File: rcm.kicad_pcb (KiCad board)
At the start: 2 copper layers, 140 x 70 mm, 158 parts, among them Y1 8MHz, Y2 32.768kHz

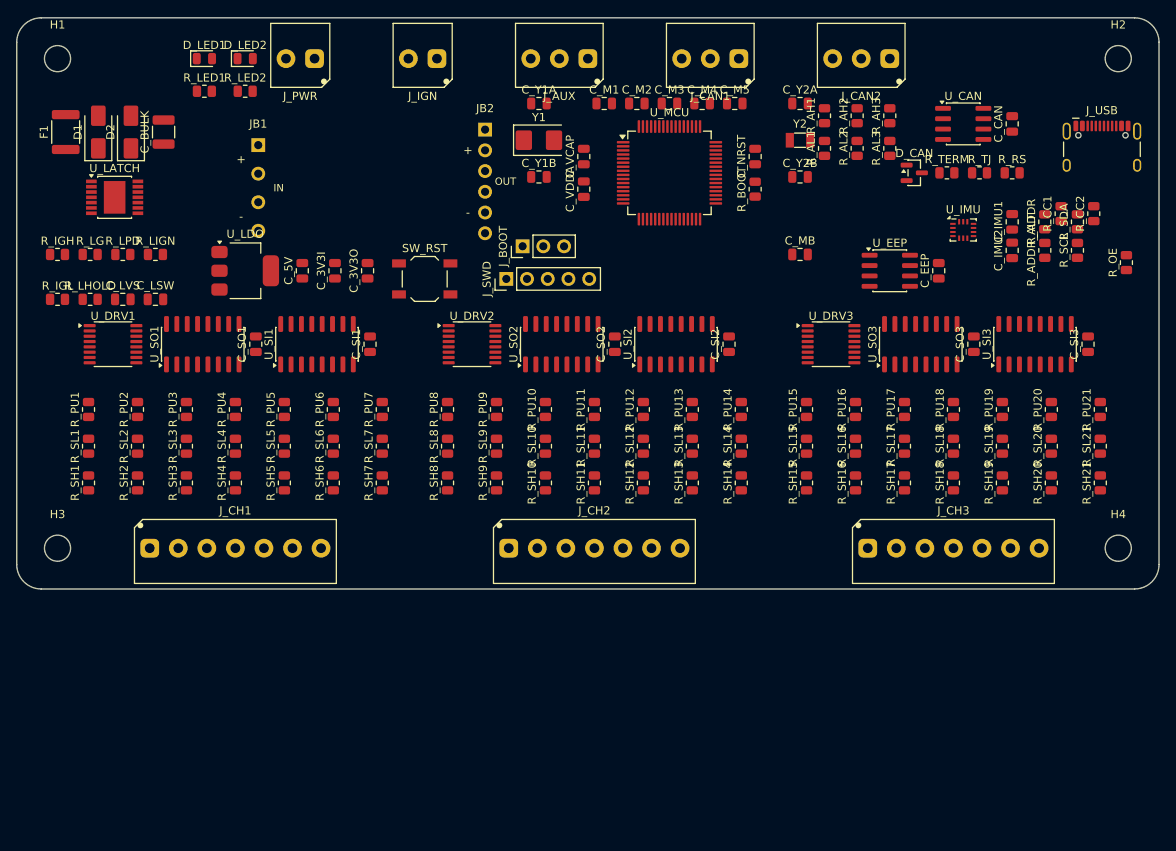
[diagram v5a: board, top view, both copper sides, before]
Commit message: rcm: board routed - 414/414 nets, 0 unconnected
Round 1 routed 413 of 414 in 63 seconds and needed NO placement changes for
congestion, which was the thing we expected to fight. The spread-out layout did
its job.

Two real issues came out of it:

- Starved thermals: a ground pad reaching the pour through one narrow neck. On
  reflow-soldered parts the relief buys nothing, so a solid connection is both
  the fix and the better design. Which pads get starved changes on every
  re-route, so fix_starved_thermals.py reads the DRC report rather than
  hard-coding them - re-run it after every route.
- USB_CC1 was unroutable: the CC pin sits in a 0.5mm-pitch pad row with no
  escape gap and I had placed its resistor on the side where the second pad row
  blocks the way. Moved to the connector's open side; round 2 then routed all
  414 nets with 0 unconnected.

Left open deliberately, per the user: rotate the USB-C 90 degrees anticlockwise
so it opens out of the east edge instead of the north. That also clears the two
remaining courtyard errors (H2 against the relocated CC resistors), so fixing
them now would be wasted work.

Co-Authored-By: Claude Opus 5 <noreply@anthropic.com>
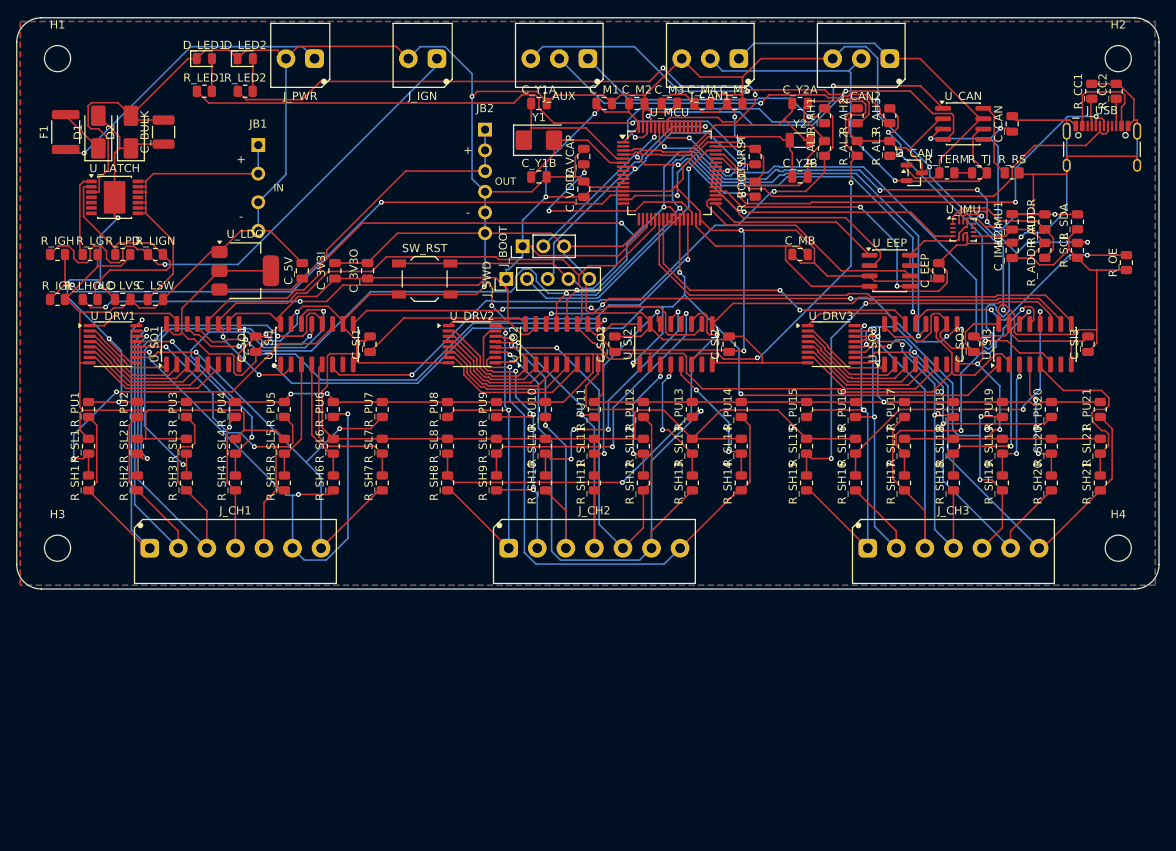
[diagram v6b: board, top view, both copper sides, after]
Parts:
- moved R_CC1 15.5 mm to (131.8, 9.00)
- moved R_CC2 15.2 mm to (134.8, 9.00)
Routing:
- net GND: track 0.00 -> 863.1 mm, vias 0 -> 10
- net +3V3: track 0.00 -> 413.6 mm, vias 0 -> 9
- net +12V_P: track 0.00 -> 214.8 mm, vias 0 -> 8
- net SR_OE_N: track 0.00 -> 159.7 mm, vias 0 -> 6
- net SR_SCK: track 0.00 -> 150.3 mm, vias 0 -> 2
- net SR_RCLK: track 0.00 -> 138.6 mm, vias 0 -> 4
- net SR_PL: track 0.00 -> 123.6 mm, vias 0 -> 4
- net IMU_SCL: track 0.00 -> 95.1 mm, vias 0 -> 3
- net LATCH_HOLD: track 0.00 -> 87.1 mm, vias 0 -> 4
- net LED2: track 0.00 -> 81.0 mm, vias 0 -> 2
- net ASNS1: track 0.00 -> 80.2 mm, vias 0 -> 2
- net IGN_SENSE: track 0.00 -> 80.1 mm, vias 0 -> 2
- net LED1: track 0.00 -> 77.0 mm, vias 0 -> 2
- net CH13: track 0.00 -> 71.3 mm, vias 0 -> 2
- net CH14: track 0.00 -> 69.0 mm, vias 0 -> 1
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- added copper zone on B.Cu, net GND
- added copper zone on F.Cu, net GND

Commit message: rcm: round 3 - USB-C rotated +90, headers and southern resistors nudged
Applies the three requested changes: J_USB rotated 0 -> +90 so it opens out of
the east edge, J_SWD and J_BOOT moved right and down to clear the buck, and all
southern resistor rows moved down 2mm to close the gap to their terminals.

Rotating the USB-C moves its CC pads, and all 16 signal pads share one local y,
so there is no asymmetry to predict orientation from. The new pad positions were
read back off the placed board rather than predicted - local pad coordinates do
not change under rotation, only the footprint angle. The CC resistors, I2C
pull-ups and CAN slope resistor all moved as a knock-on.

Routed 414/414 with 0 unconnected, 2346 segments and vias. After the usual
starved-thermal pass the board is at 0 errors.

Still unverified and worth an eyeball: which way the USB opening actually faces.
The body sits east of the pad row, which implies the cable entry is on the east
edge as intended, but that is inference not verification. If it faces inward the
fix is 270 rather than 90.

Co-Authored-By: Claude Opus 5 <noreply@anthropic.com>
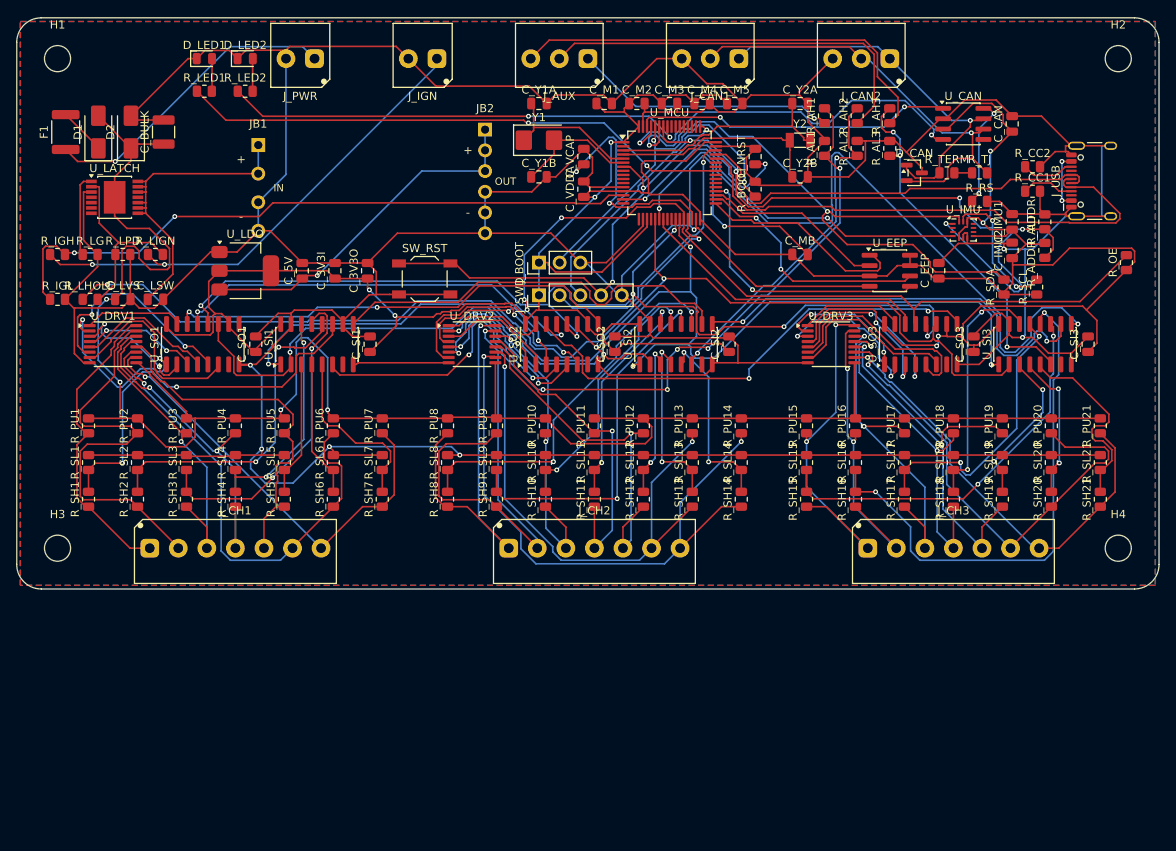
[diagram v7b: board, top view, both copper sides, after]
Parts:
- moved R_CC1 14.2 mm to (124.5, 21.2), turned to 0 degrees
- moved R_CC2 13.8 mm to (124.5, 18.2), turned to 0 degrees
- moved R_SDA 12.0 mm to (121.0, 33.0)
- moved R_SCL 6.73 mm to (125.0, 33.0)
- moved R_RS 5.32 mm to (118.0, 22.5)
- moved J_SWD 4.47 mm to (64.0, 34.0)
- moved J_USB 3.00 mm to (133.0, 20.0), turned to 90 degrees
- moved J_BOOT 2.83 mm to (64.0, 30.0)
- moved R_PU1 2.00 mm to (8.80, 50.0)
- moved R_PU10 2.00 mm to (64.8, 50.0)
- moved R_PU11 2.00 mm to (70.8, 50.0)
- moved R_PU12 2.00 mm to (76.8, 50.0)
- moved R_PU13 2.00 mm to (82.8, 50.0)
- moved R_PU14 2.00 mm to (88.8, 50.0)
- moved R_PU15 2.00 mm to (96.8, 50.0)
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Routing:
- net GND: track 863.1 -> 814.1 mm, vias 10 -> 8
- net +3V3: track 413.6 -> 377.7 mm, vias 9 -> 8
- net IMU_SCL: track 95.1 -> 66.6 mm, vias 3 -> 5
- net +12V_P: track 214.8 -> 242.6 mm, vias 8 -> 4
- net SR_MISO: track 59.6 -> 86.6 mm, vias 0 -> 2
- net SNS16: track 39.9 -> 64.4 mm
- net LED2: track 81.0 -> 56.7 mm
- net ASNS1: track 80.2 -> 98.7 mm, vias 2 -> 6
- net SNS4: track 44.4 -> 27.2 mm
- net CH9: track 41.6 -> 58.7 mm, vias 3 -> 1
- net SR_PL: track 123.6 -> 138.5 mm
- net CH1: track 50.7 -> 37.3 mm, vias 1 -> 0
- net SR_OE_N: track 159.7 -> 146.6 mm, vias 6 -> 5
- net IMU_SDO: track 18.0 -> 30.9 mm, vias 0 -> 2
- net CH3: track 50.7 -> 38.6 mm
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
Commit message: rcm: board fully routed and DRC-clean - 414/414 nets, 0 errors
Round 5 routes every net with 0 unconnected and, after the thermal pass, 0 DRC
errors. 2214 segments and vias, ground poured both sides. Only silkscreen
warnings remain.

Two real faults fixed, both found by checking rather than assuming:

- The USB-C opening sat 2.8mm INSIDE the board edge. The +90 rotation pointed it
  east correctly, but a plug would have fouled the PCB before seating. Moved
  flush. The resulting NEAR EDGE lint warning is the correct outcome for an edge
  connector.
- BOOT0 failed three consecutive runs with a byte-identical stub and identical
  score. I dismissed it as a stochastic router artifact and suggested retrying;
  that was wrong. Identical output is the tell that it is deterministic. The
  cause was real: the five MCU decoupling caps left a 0.6mm slot as the only
  escape from pad 60 on the 0.5mm-pitch QFP edge. Fixed by leaving a gap in that
  row and putting R_BOOT directly north of the pad.

Also found: fix_starved_thermals.py silently skips through-hole pads. Its parser
expects "Pad N [NET] of REF" but the DRC report writes "PTH pad N ..." for THT,
so it reports nothing to do while the violations remain. J_SWD pad 5 was set
solid by hand. Worth fixing in the shared tool.

Co-Authored-By: Claude Opus 5 <noreply@anthropic.com>
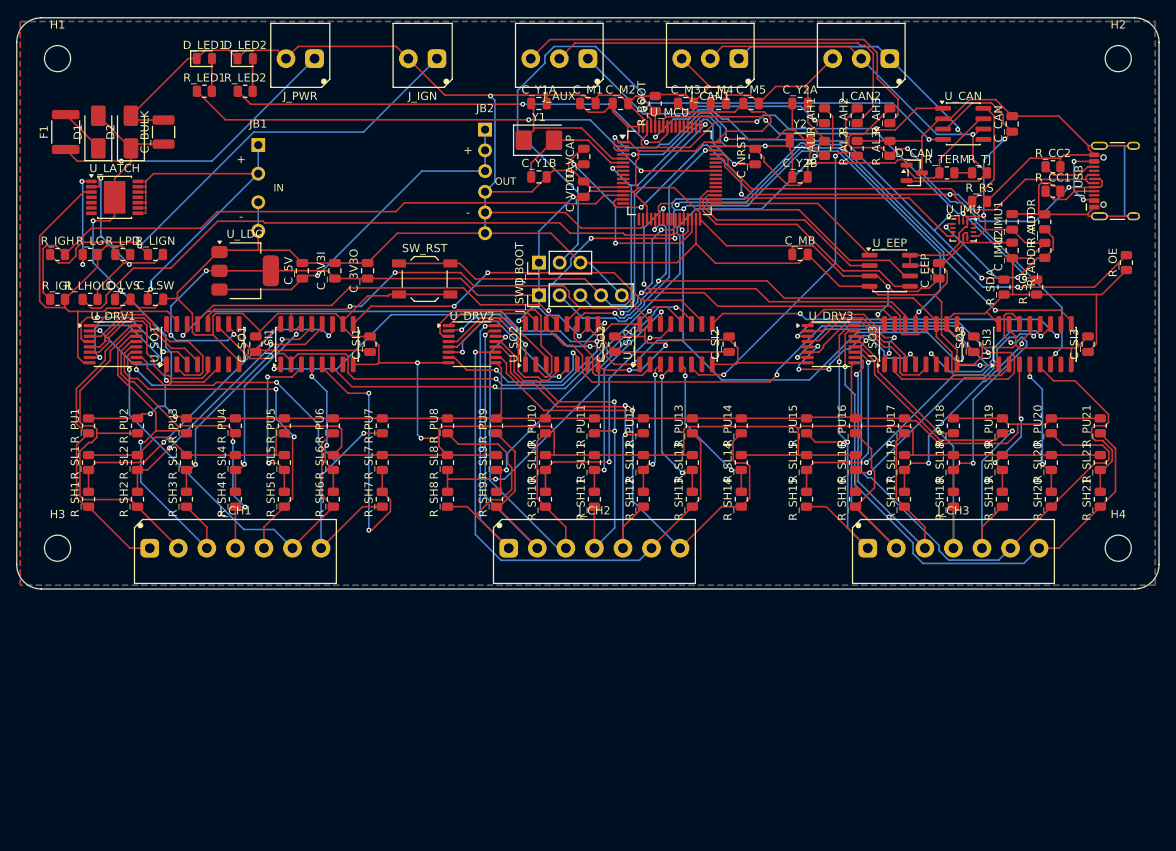
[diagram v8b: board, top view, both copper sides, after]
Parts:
- moved R_BOOT 16.1 mm to (78.2, 10.5)
- moved J_USB 2.80 mm to (135.8, 20.0)
- moved R_CC1 2.50 mm to (127.0, 21.2)
- moved R_CC2 2.50 mm to (127.0, 18.2)
- moved C_M1 2.00 mm to (70.0, 10.5)
- moved C_M2 2.00 mm to (74.0, 10.5)
- moved C_M3 2.00 mm to (82.0, 10.5)
- moved C_M4 2.00 mm to (86.0, 10.5)
- moved C_M5 2.00 mm to (90.0, 10.5)
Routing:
- net SR_OE_N: track 146.6 -> 193.8 mm, vias 5 -> 6
- net +12V_P: track 242.6 -> 206.7 mm, vias 4 -> 5
- net SNS16: track 64.4 -> 34.7 mm
- net GND: track 814.1 -> 843.4 mm, vias 8 -> 5
- net DRV17: track 19.6 -> 48.6 mm
- net +3V3: track 377.7 -> 352.5 mm, vias 8 -> 10
- net SR_MISO: track 86.6 -> 65.1 mm
- net SR_PL: track 138.5 -> 118.4 mm, vias 4 -> 5
- net IMU_SDA: track 76.8 -> 58.7 mm, vias 2 -> 3
- net DRV21: track 21.5 -> 37.5 mm, vias 0 -> 2
- net SR_RCLK: track 128.2 -> 113.4 mm, vias 6 -> 5
- net ASNS1: track 98.7 -> 84.0 mm, vias 6 -> 2
- net CH14: track 74.8 -> 60.5 mm, vias 2 -> 1
- net DRV10: track 14.4 -> 26.3 mm
- net SNS3: track 40.1 -> 28.4 mm
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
